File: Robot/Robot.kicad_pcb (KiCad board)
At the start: 2 copper layers, 100 x 100 mm, 33 parts, among them J1 Barrel_Jack, J10 Conn_01x03_Pin, J11 Stepper_2, J2 Conn_01x02_Pin, J3 Stepper_2, J4 UltraSonic, J5 MotorController, J6 Range, J7 Conn_01x04_Pin, J8 Conn_01x03_Pin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

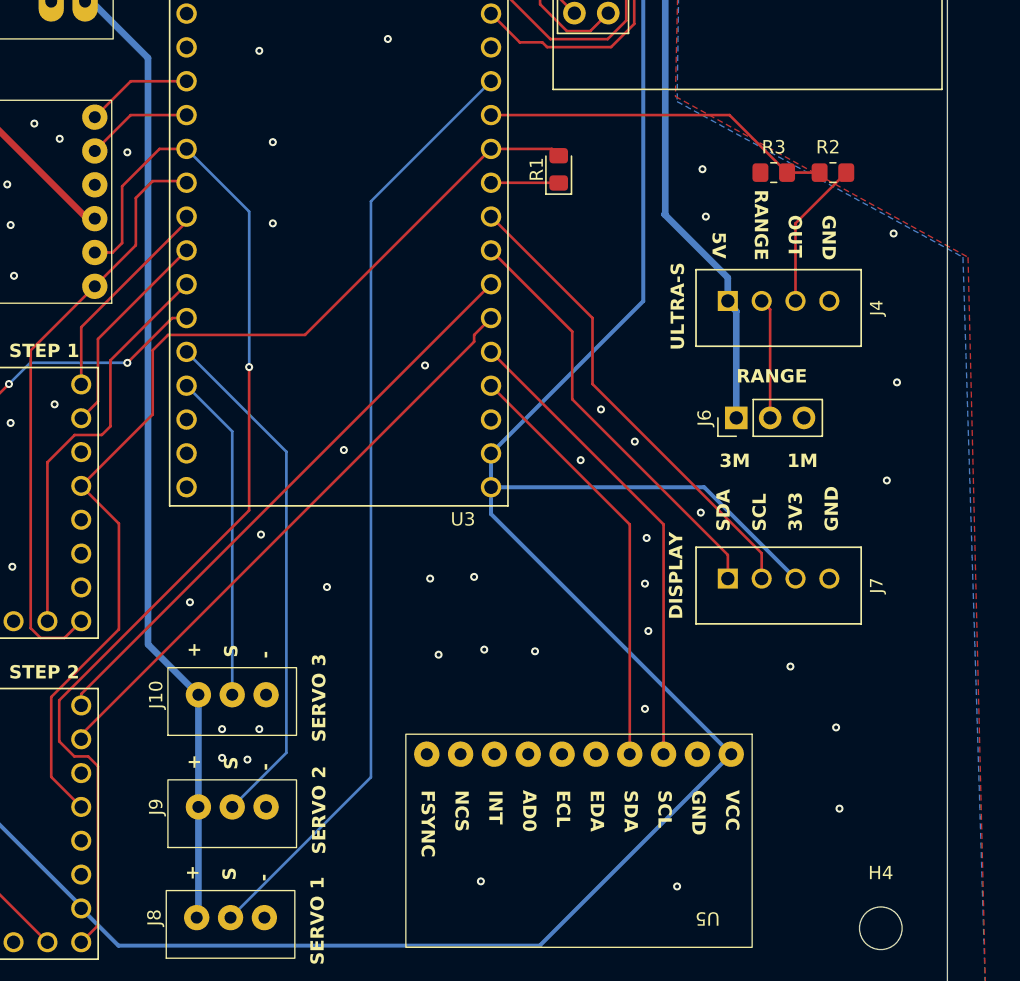
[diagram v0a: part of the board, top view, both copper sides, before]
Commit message: Updated robot and created 0402 test pcb
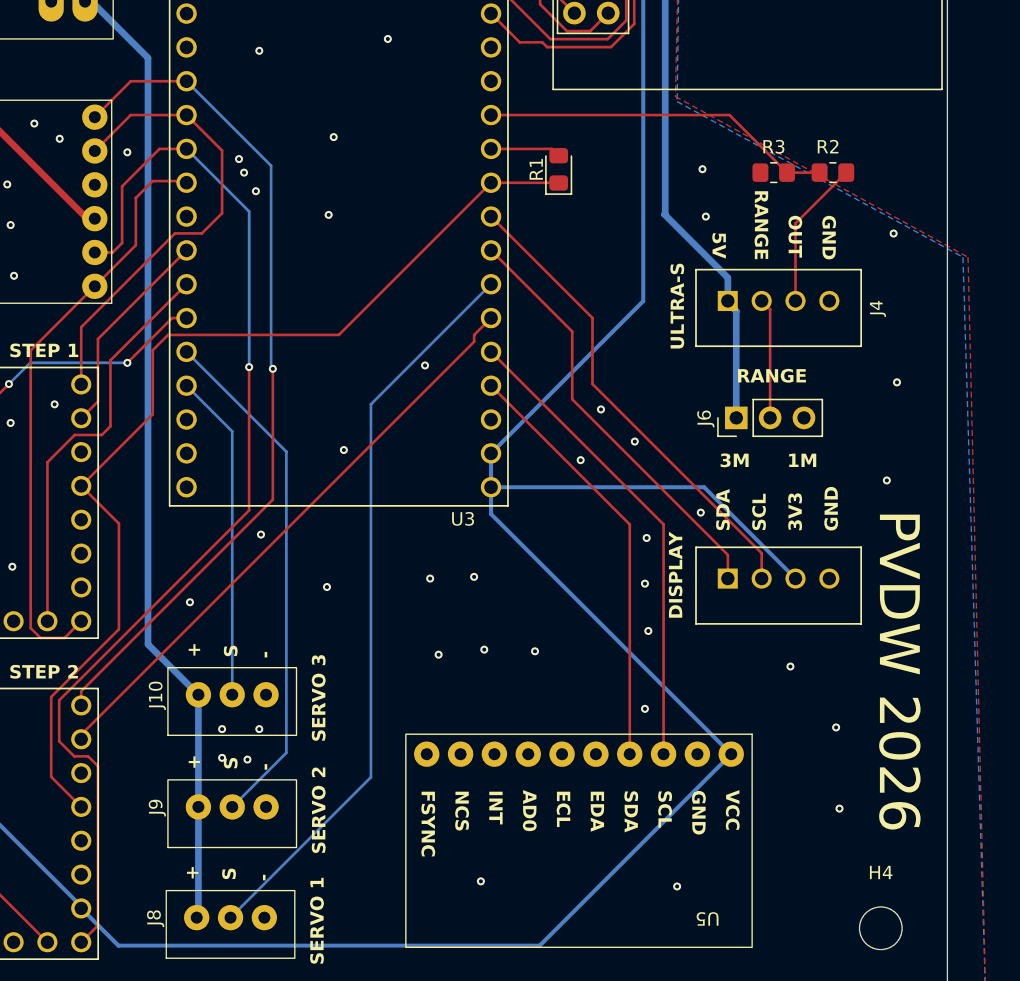
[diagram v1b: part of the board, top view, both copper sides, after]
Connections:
- R1 pad 1: Net-(U3-GPIO17) -> /S12_UART
- R1 pad 2: /S12_UART -> Net-(U3-GPIO18)
- U2 pad 9: /S2_DIR -> /MC_IN4_S2_DIR
- U3 pad J1_10: Net-(U3-GPIO17) -> /S12_UART
- U3 pad J1_11: /S12_UART -> Net-(U3-GPIO18)
- U3 pad J1_13: /SIG_SERVO_1 -> unconnected-(U3-GPIO3-PadJ1_13)
- U3 pad J1_7: /S2_DIR -> /SIG_SERVO_1
- U3 pad J3_12: /MC_IN3 -> /MC_IN3_S1_DIR
- U3 pad J3_13: /MC_IN4 -> /MC_IN4_S2_DIR
- U3 pad J3_9: /S1_DIR -> unconnected-(U3-MTCK/GPIO39-PadJ3_9)
- U7 pad 9: /S1_DIR -> /MC_IN3_S1_DIR
- U9 pad 5: /MC_IN3 -> /MC_IN3_S1_DIR
- U9 pad 6: /MC_IN4 -> /MC_IN4_S2_DIR
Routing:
- net /MC_IN4_S2_DIR: track 0.00 -> 63.5 mm, vias 0 -> 1
- net /S2_DIR: track 44.4 -> 0.00 mm
- net /MC_IN3_S1_DIR: track 0.00 -> 34.9 mm
- net /S1_DIR: track 15.9 -> 0.00 mm
- net /SIG_SERVO_1: track 70.9 -> 55.7 mm
- net /MC_IN4: track 8.01 -> 0.00 mm
- net /MC_IN3: track 8.01 -> 0.00 mm
- net Net-(U3-GPIO18): track 0.00 -> 5.29 mm
- net Net-(U3-GPIO17): track 5.09 -> 0.00 mm
- net /S12_UART: track 77.7 -> 76.4 mm
- net GND: vias 76 -> 79
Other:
- board text added: "PVDW 2026"

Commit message: New versions for Robot PCBs
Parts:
- removed R2: 4k7, Resistor_SMD:R_0805_2012Metric_Pad1.20x1.40mm_HandSolder
- removed R3: 10k, Resistor_SMD:R_0805_2012Metric_Pad1.20x1.40mm_HandSolder
- C1, C2, R1: moved to B.Cu
- J2, U8: footprint PVDW_custom:Connector_1x2_p2.54_vertical -> PVDW_custom:screw_block_2pin
- moved C2 27.5 mm to (179.6, 90.9), turned to -90 degrees
- moved C1 25.8 mm to (179.6, 86.0), turned to 90 degrees
- moved U1 24.7 mm to (185.0, 89.6), turned to 90 degrees
- moved U8 14.0 mm to (106.6, 67.5), turned to 90 degrees
- moved F1 12.9 mm to (121.7, 66.4), turned to 90 degrees
- moved U4 7.95 mm to (136.1, 67.0), turned to 90 degrees
- moved U3 7.75 mm to (162.1, 82.0)
- moved J2 3.70 mm to (106.6, 91.1)
- moved J4 2.18 mm to (187.2, 100.6)
- moved J6 1.78 mm to (184.0, 108.5)
- moved J7 1.66 mm to (187.2, 120.9)
- moved J1 1.16 mm to (115.0, 76.1)
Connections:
- net Net-(U3-GPIO18) renamed /UART_TX
- F1 pad 1: +24V -> VBat
- F1 pad 2: +24V -> Vin
- J1 pad 1: +24V -> VBat
- J10 pad 1: +5V -> GND
- J10 pad 3: GND -> +5V
- J2 pad 2: +24V -> VBat
- J4 pad 1: +5V -> +3.3V
- J4 pad 3: Net-(J4-Pin_3) -> /US_OUT
- J6 pad 1: +5V -> +3.3V
- J8 pad 1: +5V -> GND
- J8 pad 3: GND -> +5V
- J9 pad 1: +5V -> GND
- J9 pad 3: GND -> +5V
- U2 pad 11: unconnected-(U2-PDN-Pad11) -> /S12_UART
- U2 pad 12: /S12_UART -> unconnected-(U2-UART-Pad12)
- U2 pad 8: +24V -> VDC
- U3 pad J1_13: unconnected-(U3-GPIO3-PadJ1_13) -> /IMU_INT
- U4 pad 1: +24V -> VDC
- U5 pad 8: unconnected-(U5-INT-Pad8) -> /IMU_INT
- U7 pad 11: unconnected-(U7-PDN-Pad11) -> /S12_UART
- U7 pad 12: /S12_UART -> unconnected-(U7-UART-Pad12)
- U7 pad 8: +24V -> VDC
- U8 pad 1: +24V -> VDC
- U8 pad 2: +24V -> Vin
- U9 pad 12: unconnected-(U9-EEP-Pad12) -> +3.3V
- U9 pad 3: +24V -> GND
- U9 pad 4: GND -> VDC
- U9 pad 7: +3.3V -> unconnected-(U9-ULT-Pad7)
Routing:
- net +24V: track 173.2 -> 0.00 mm
- net VDC: track 0.00 -> 132.7 mm
- net +5V: track 199.5 -> 140.8 mm
- net /IMU_INT: track 0.00 -> 47.4 mm, vias 0 -> 2
- net +3.3V: track 238.1 -> 275.3 mm, vias 0 -> 1
- net VBat: track 0.00 -> 32.6 mm
- net /NRF_CLK: track 10.2 -> 41.0 mm
- net /NRF_CE: track 10.2 -> 37.5 mm
- net Vin: track 0.00 -> 20.8 mm
- net /NRF_MISO: track 10.2 -> 30.8 mm
- net GND: track 0.00 -> 15.3 mm, vias 79 -> 89
- net /NRF_IRQ: track 12.4 -> 24.4 mm
- net Net-(J4-Pin_3): track 11.2 -> 0.00 mm
- net /MC_IN2_S2_EN: track 82.4 -> 71.1 mm, vias 1 -> 0
- net /SIG_SERVO_1: track 55.7 -> 65.9 mm
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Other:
- board text added: "+"
- board text added: "+3V3"
- board text added: "+5V"
- board text added: "-"
- board text added: "5A"
- board text added: "OnOff"
- board text added: "SDA"
- board text added: "Vin"

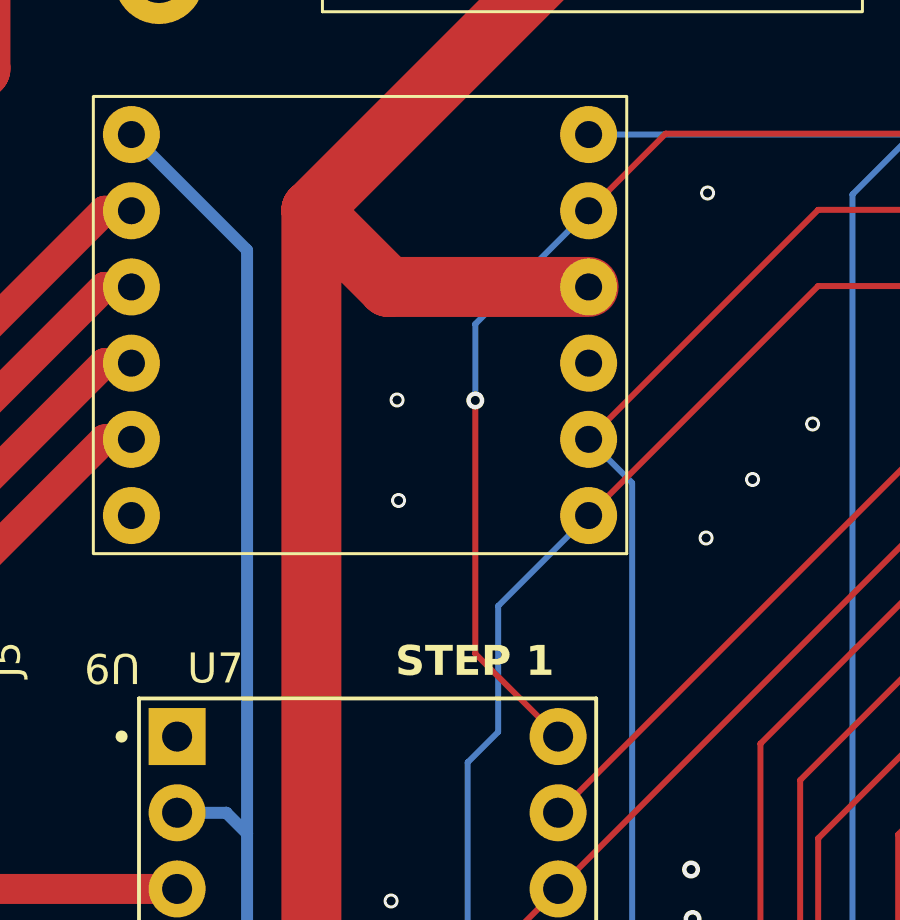
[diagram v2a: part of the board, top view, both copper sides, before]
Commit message: Fixed VCC-GND mixup on drv8833
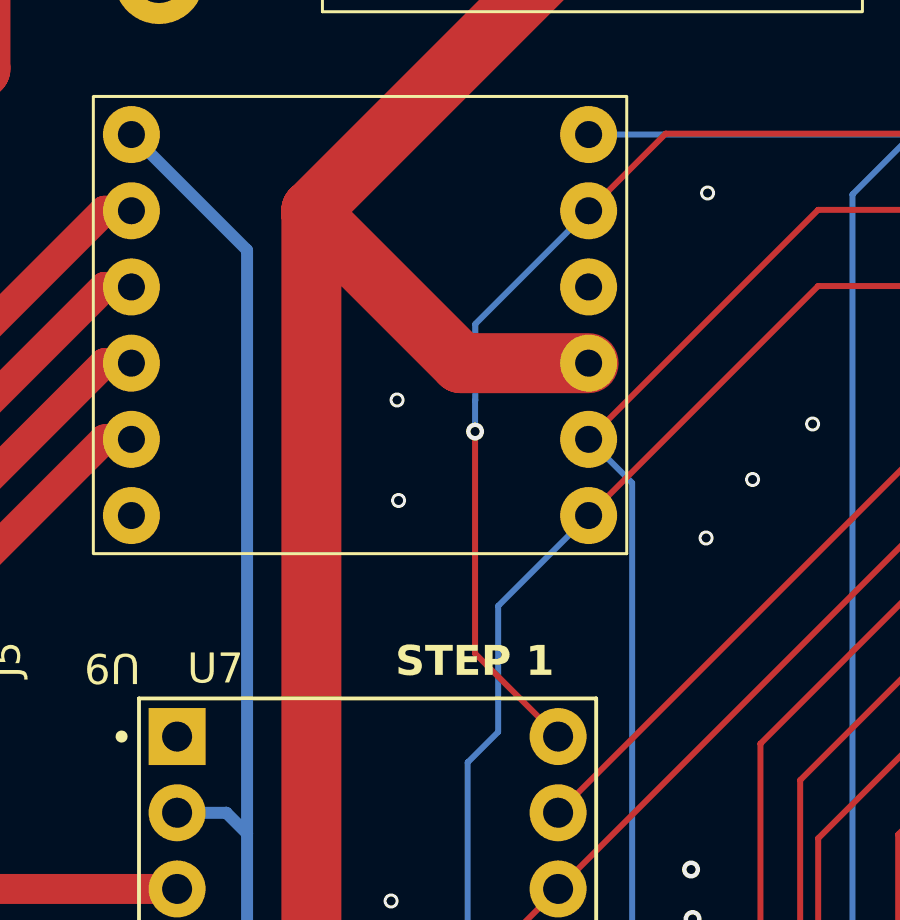
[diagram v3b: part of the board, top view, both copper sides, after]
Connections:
- U9 pad 3: GND -> VDC
- U9 pad 4: VDC -> GND
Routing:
- net VDC: track 132.7 -> 133.8 mm
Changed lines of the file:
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@@
 			(layers "*.Cu" "*.Mask")
 			(remove_unused_layers no)
-			(net 1 "GND")
-			(pinfunction "GND")
+			(net 69 "VDC")
+			(pinfunction "VCC")
 			(pintype "power_in")
 		)
@@
 			(layers "*.Cu" "*.Mask")
 			(remove_unused_layers no)
-			(net 69 "VDC")
-			(pinfunction "VCC")
+			(net 1 "GND")
+			(pinfunction "GND")
 			(pintype "power_in")
 		)
@@
 	)
 	(segment
-		(start 132.207 101.407833)
-		(end 132.207 92.964)
+		(start 132.2 94)
+		(end 132.2 101.400833)
 		(width 0.2)
 		(layer "F.Cu")
@@
 	)
 	(segment
-		(start 134.9675 104.168333)
-		(end 132.207 101.407833)
+		(start 132.2 101.400833)
+		(end 134.9675 104.168333)
 		(width 0.2)
 		(layer "F.Cu")
@@
 	)
 	(via
-		(at 132.207 92.964)
+		(at 132.2 94)
 		(size 0.6)
 		(drill 0.3)
@@
 	)
 	(segment
+		(start 132.2 94)
+		(end 132.2 92.971)
+		(width 0.2)
+		(layer "B.Cu")
+		(net 42)
+	)
+	(segment
 		(start 132.207 90.419667)
 		(end 135.985 86.641667)
@@
 	)
 	(segment
+		(start 132.2 92.971)
+		(end 132.207 92.964)
+		(width 0.2)
+		(layer "B.Cu")
+		(net 42)
+	)
+	(segment
 		(start 185.928 120.396)
 		(end 185.928 118.328)
@@
 	)
 	(segment
+		(start 135.985 91.721667)
+		(end 131.721667 91.721667)
+		(width 2)
+		(layer "F.Cu")
+		(net 69)
+	)
+	(segment
 		(start 123.333817 146.05)
 		(end 122.2675 146.05)
@@
 	)
 	(segment
+		(start 126.743333 86.743333)
+		(end 126.743333 86.616667)
+		(width 2)
+		(layer "F.Cu")
+		(net 69)
+	)
+	(segment
 		(start 140.462 76.708)
 		(end 143.002 76.708)
@@
 	)
 	(segment
-		(start 129.308333 89.181667)
-		(end 126.743333 86.616667)
+		(start 131.721667 91.721667)
+		(end 126.743333 86.743333)
 		(width 2)
 		(layer "F.Cu")
@@
 		(width 2)
 		(layer "F.Cu")
-		(net 69)
-	)
-	(segment
-		(start 135.985 89.181667)
-		(end 129.308333 89.181667)
-		(width 2)
-		(layer "F.Cu")

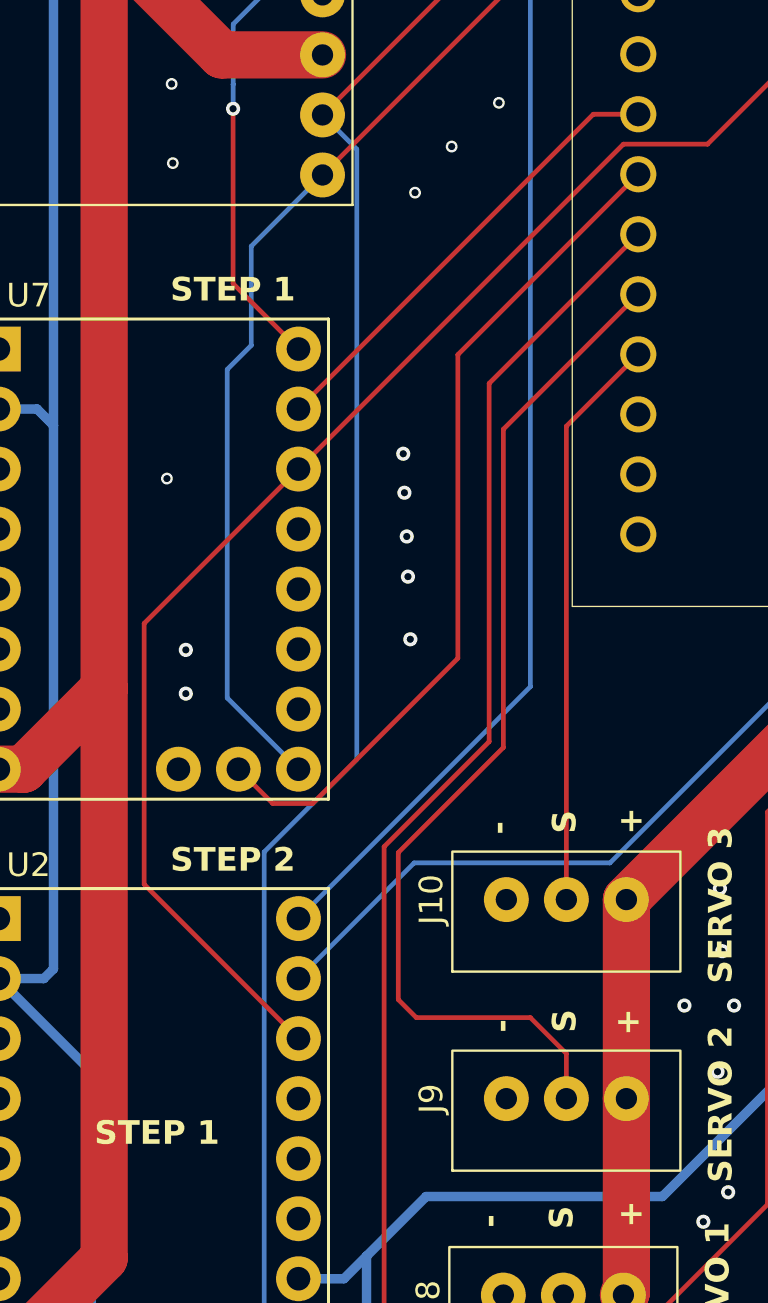
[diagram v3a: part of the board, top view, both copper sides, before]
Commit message: Minor bugfixes in Robot PCB (UART connected to the wrong pin of the stepper driver)
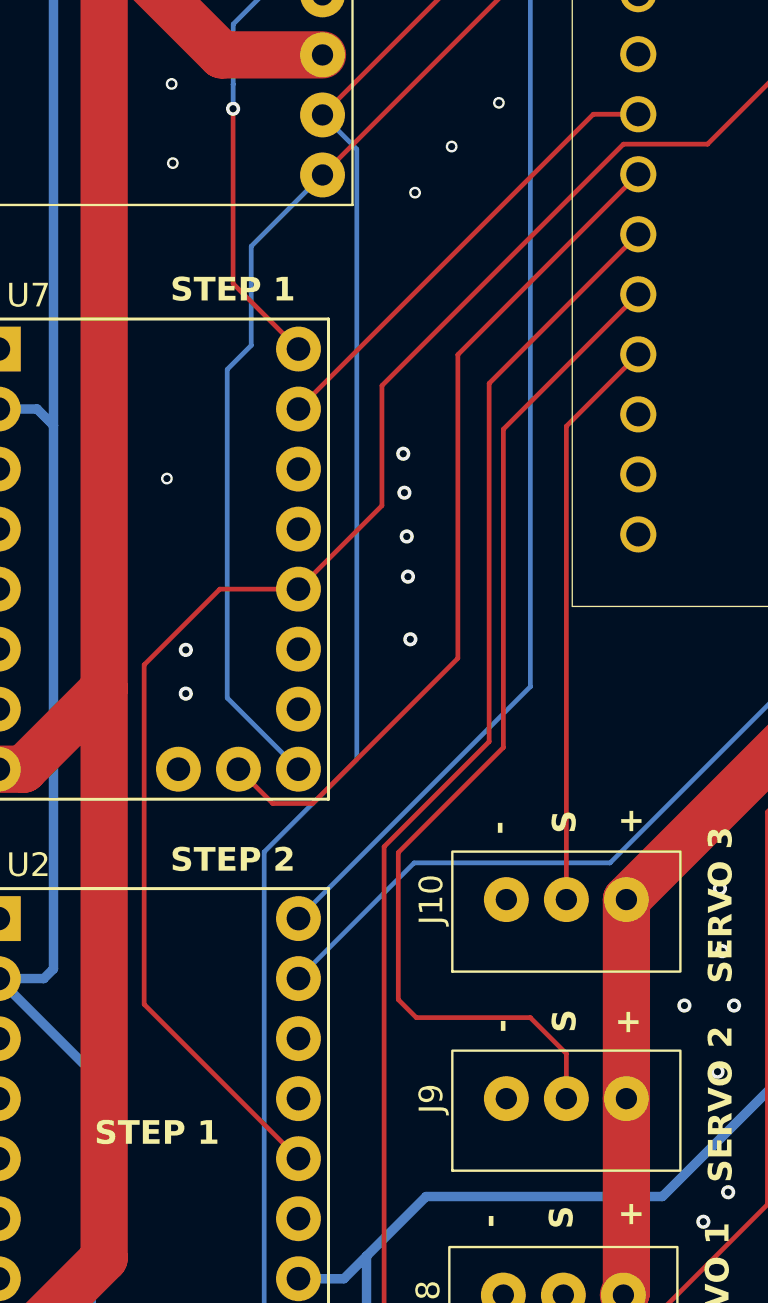
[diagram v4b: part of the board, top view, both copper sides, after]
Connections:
- U2 pad 11: /S12_UART -> unconnected-(U2-SPRD-Pad11)
- U2 pad 13: unconnected-(U2-SPRD-Pad13) -> /S12_UART
- U7 pad 11: /S12_UART -> unconnected-(U7-SPRD-Pad11)
- U7 pad 13: unconnected-(U7-SPRD-Pad13) -> /S12_UART
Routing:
- net /S12_UART: track 77.8 -> 84.9 mm
